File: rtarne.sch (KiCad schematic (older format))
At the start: 6 parts, among them J2 4PIN, U1 ProMicro

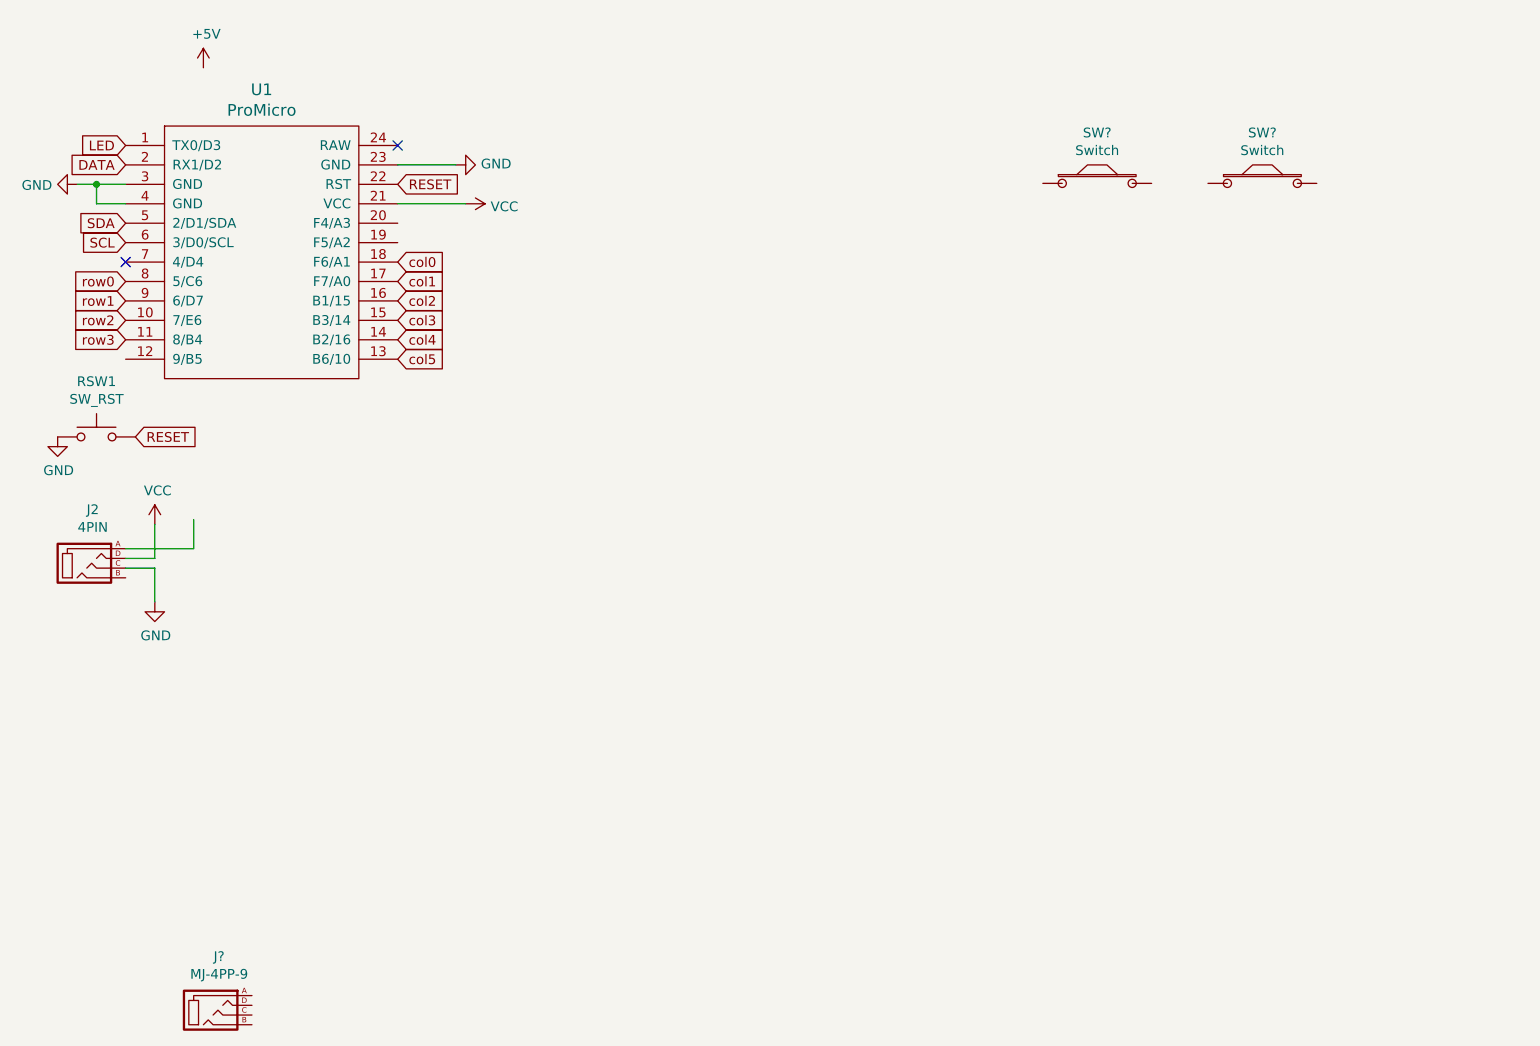
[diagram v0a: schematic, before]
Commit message: Add switches in electric schema
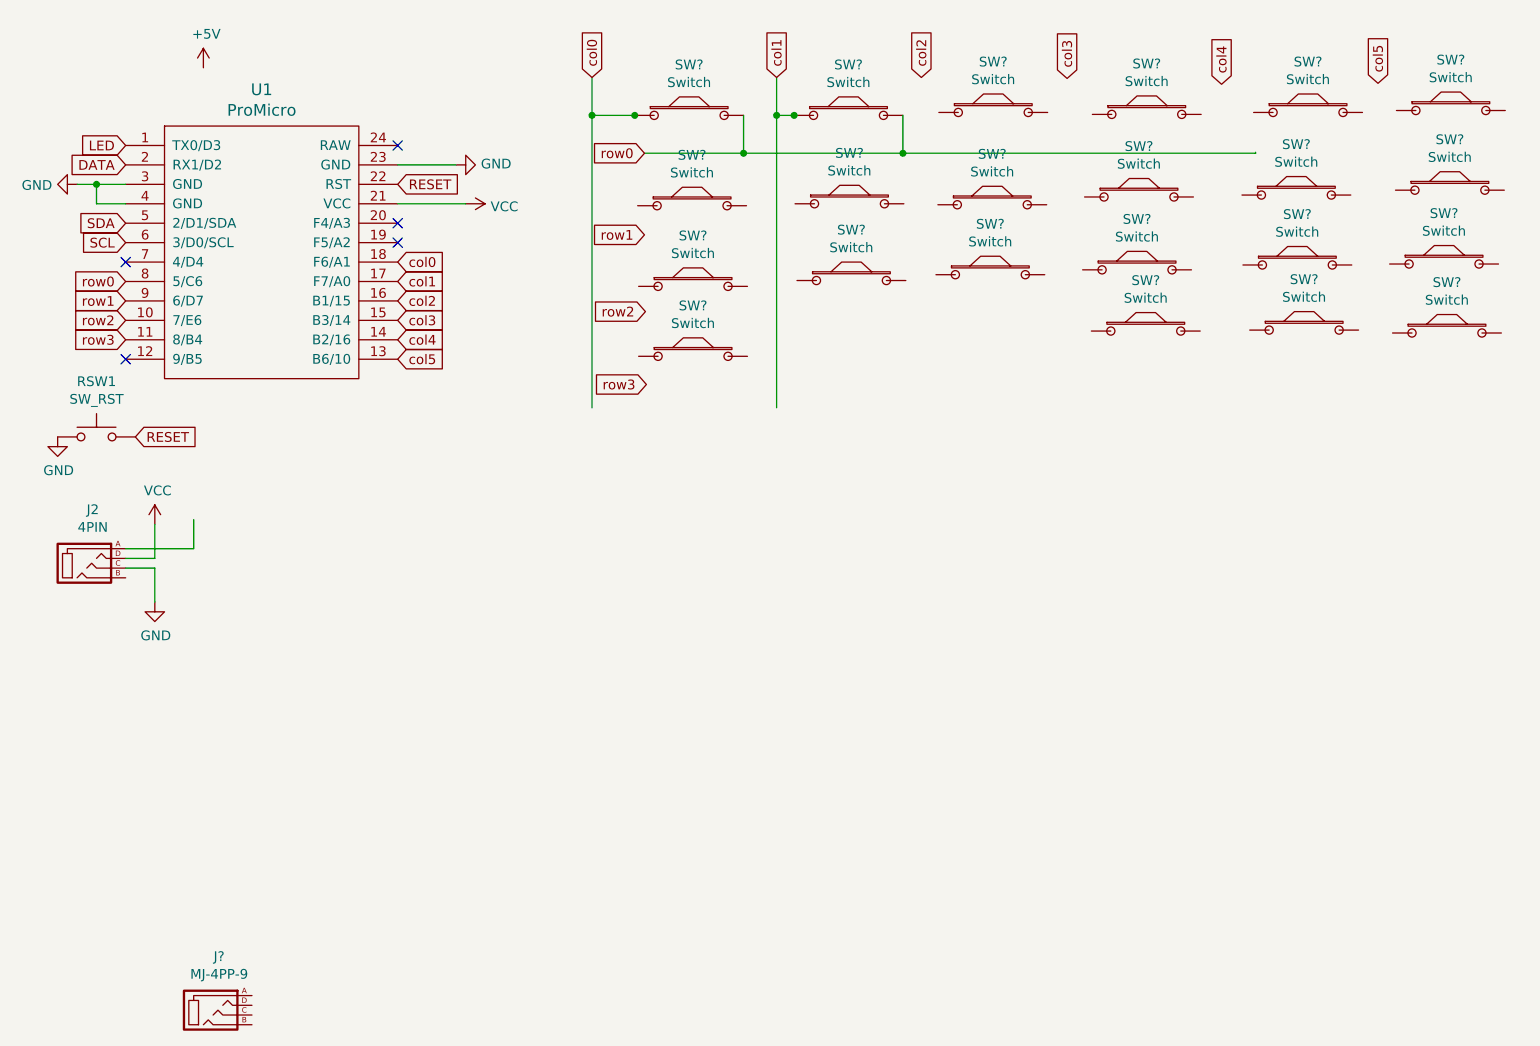
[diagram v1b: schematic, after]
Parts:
- added SW? (x20): Switch, RTA-80:SW_RTA80, symbol rta80:Switch
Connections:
- wire segments 12 -> 26
- no-connect marks 2 -> 5
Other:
- moved on the sheet: SW?

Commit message: Recreate schema
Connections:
- wire segments 26 -> 27
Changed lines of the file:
@@
 Text GLabel 3820 1610 0    50   Input ~ 0
 row1
-Text GLabel 3825 2005 0    50   Input ~ 0
-row2
 Text GLabel 3830 2380 0    50   Input ~ 0
 row3
@@
 	1    0    0    -1
 $EndComp
+Wire Wire Line
+	3820 1610 8350 1610
+Text GLabel 3825 2005 0    50   Input ~ 0
+row2
 $EndSCHEMATC
